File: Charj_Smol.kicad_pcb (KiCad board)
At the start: 2 copper layers, 15 x 15 mm, 18 parts, among them J1 Battery Connector, Q1 PMN30XPEX, U1 MCP73831-2-OT, U2 LC709203FXE-05MH

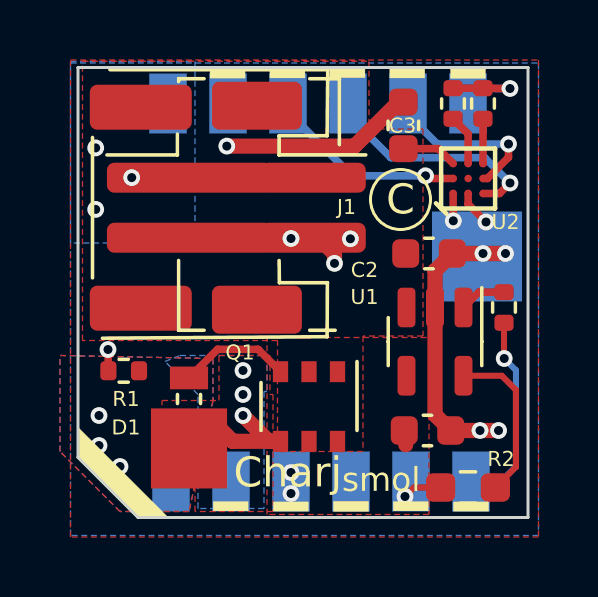
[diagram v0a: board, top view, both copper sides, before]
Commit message: Silkscreen tidying; still Rev C
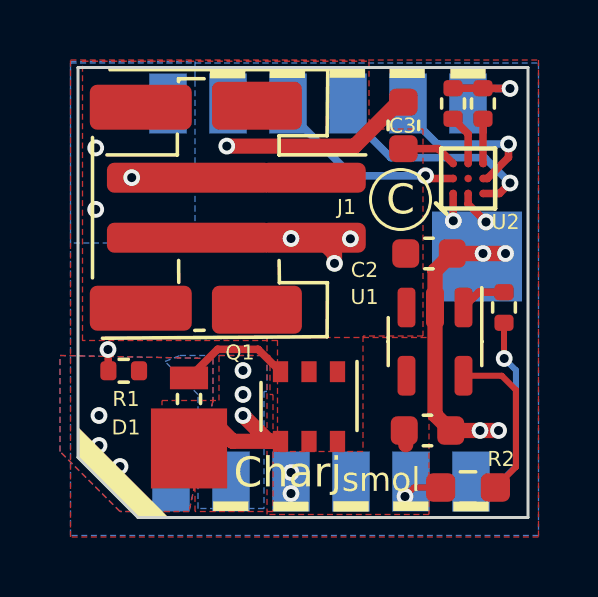
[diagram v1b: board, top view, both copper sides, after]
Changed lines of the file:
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@@
       (effects (font (size 1 1) (thickness 0.15)))
     )
-    (fp_line (start 2.51 -4.2) (end 3.5 -4.2) (layer "F.SilkS") (width 0.12))
+    (fp_line (start -4.15 -4.5) (end 3.1125 -4.5) (layer "F.SilkS") (width 0.12))
+    (fp_line (start 1.4894 -2.3) (end 1.4894 -1.66) (layer "F.SilkS") (width 0.12))
+    (fp_line (start 1.4894 -1.66) (end 4.3794 -1.66) (layer "F.SilkS") (width 0.12))
+    (fp_line (start -4.7306 -2.24) (end -4.7306 2.44) (layer "F.SilkS") (width 0.12))
+    (fp_line (start 3.1125 -4.5) (end 3.0894 -2.3) (layer "F.SilkS") (width 0.12))
+    (fp_line (start 3.0894 -2.3) (end 1.4894 -2.3) (layer "F.SilkS") (width 0.12))
+    (fp_line (start -4.4 4.45) (end 3.0894 4.4) (layer "F.SilkS") (width 0.12))
+    (fp_line (start -1.86 -4.2) (end -1.86 -4.1) (layer "F.SilkS") (width 0.12))
+    (fp_line (start 3.0894 4.4) (end 3.1 2.6) (layer "F.SilkS") (width 0.12))
+    (fp_line (start -1.8542 2.5908) (end -1.86 1.86) (layer "F.SilkS") (width 0.12))
+    (fp_line (start -1.01 -4.2) (end -1.86 -4.2) (layer "F.SilkS") (width 0.12))
+    (fp_line (start -1.9 -1.66) (end -4.25 -1.66) (layer "F.SilkS") (width 0.12))
     (fp_line (start -1.9 -1.66) (end -1.9 -2.35) (layer "F.SilkS") (width 0.12))
-    (fp_line (start 1.4894 -2.3) (end 1.4894 -1.66) (layer "F.SilkS") (width 0.12))
+    (fp_line (start -1.01 4.185) (end -1.3208 4.191) (layer "F.SilkS") (width 0.12))
+    (fp_line (start 3.1 2.6) (end 1.5 2.6) (layer "F.SilkS") (width 0.12))
     (fp_line (start 1.5 2.6) (end 1.4894 1.86) (layer "F.SilkS") (width 0.12))
-    (fp_line (start -4.15 -4.5) (end 3.1125 -4.5) (layer "F.SilkS") (width 0.12))
-    (fp_line (start -1.01 4.185) (end -1.86 4.185) (layer "F.SilkS") (width 0.12))
-    (fp_line (start 3.1125 -4.5) (end 3.0894 -2.3) (layer "F.SilkS") (width 0.12))
-    (fp_line (start 3.0894 4.4) (end 3.1 2.6) (layer "F.SilkS") (width 0.12))
-    (fp_line (start 3.36 4.185) (end 2.51 4.185) (layer "F.SilkS") (width 0.12))
-    (fp_line (start 3.1 2.6) (end 1.5 2.6) (layer "F.SilkS") (width 0.12))
-    (fp_line (start -1.01 -4.2) (end -1.86 -4.2) (layer "F.SilkS") (width 0.12))
-    (fp_line (start -1.86 4.185) (end -1.86 1.86) (layer "F.SilkS") (width 0.12))
-    (fp_line (start -4.7306 -2.24) (end -4.7306 2.44) (layer "F.SilkS") (width 0.12))
-    (fp_line (start -4.4 4.45) (end 3.0894 4.4) (layer "F.SilkS") (width 0.12))
-    (fp_line (start 3.0894 -2.3) (end 1.4894 -2.3) (layer "F.SilkS") (width 0.12))
-    (fp_line (start 1.4894 -1.66) (end 4.3794 -1.66) (layer "F.SilkS") (width 0.12))
-    (fp_line (start -1.86 -4.2) (end -1.86 -4.1) (layer "F.SilkS") (width 0.12))
-    (fp_line (start -1.9 -1.66) (end -4.25 -1.66) (layer "F.SilkS") (width 0.12))
-    (fp_line (start 3.5 -4.2) (end 3.5 -2) (layer "F.SilkS") (width 0.12))
     (fp_rect (start 4.8794 -4.6) (end -5.35 4.8) (layer "F.CrtYd") (width 0.05) (fill none))
+    (fp_line (start 1.3794 -1.4) (end 0.672293 -0.9) (layer "F.Fab") (width 0.1))
+    (fp_line (start 2.9794 -3.85) (end -4.6206 -3.85) (layer "F.Fab") (width 0.1))
+    (fp_line (start 2.9794 3.25) (end 2.9794 4.05) (layer "F.Fab") (width 0.1))
+    (fp_line (start 2.9794 -3.85) (end 2.9794 -3.05) (layer "F.Fab") (width 0.1))
+    (fp_line (start -1.75 -3.875) (end -1.75 4.075) (layer "F.Fab") (width 0.1))
+    (fp_line (start 1.25 0.85) (end 1.25 1.35) (layer "F.Fab") (width 0.1))
+    (fp_line (start -1.75 4.075) (end 3.25 4.075) (layer "F.Fab") (width 0.1))
+    (fp_line (start -1.75 -3.875) (end 3.25 -3.875) (layer "F.Fab") (width 0.1))
+    (fp_line (start 1.3794 -3.05) (end 1.3794 3.25) (layer "F.Fab") (width 0.1))
+    (fp_line (start -4.6206 -3.85) (end -4.6206 4.05) (layer "F.Fab") (width 0.1))
+    (fp_line (start 1.75 -0.65) (end 1.75 -1.15) (layer "F.Fab") (width 0.1))
+    (fp_line (start 1.3794 3.25) (end 2.9794 3.25) (layer "F.Fab") (width 0.1))
     (fp_line (start 0.672293 -0.9) (end 1.3794 -0.4) (layer "F.Fab") (width 0.1))
+    (fp_line (start 1.25 -1.15) (end 1.25 -0.65) (layer "F.Fab") (width 0.1))
     (fp_line (start 1.25 -0.65) (end 1.75 -0.65) (layer "F.Fab") (width 0.1))
-    (fp_line (start 1.3794 -3.05) (end 1.3794 3.25) (layer "F.Fab") (width 0.1))
+    (fp_line (start 1.75 -1.15) (end 1.25 -1.15) (layer "F.Fab") (width 0.1))
+    (fp_line (start 1.25 1.35) (end 1.75 1.35) (layer "F.Fab") (width 0.1))
+    (fp_line (start 1.75 1.35) (end 1.75 0.85) (layer "F.Fab") (width 0.1))
+    (fp_line (start 2.9794 4.05) (end -4.6206 4.05) (layer "F.Fab") (width 0.1))
+    (fp_line (start 2.9794 -3.05) (end 1.3794 -3.05) (layer "F.Fab") (width 0.1))
+    (fp_line (start -1.042893 -0.9) (end -1.75 -0.4) (layer "F.Fab") (width 0.1))
+    (fp_line (start -1.75 -1.4) (end -1.042893 -0.9) (layer "F.Fab") (width 0.1))
     (fp_line (start 3.25 -3.875) (end 3.25 4.075) (layer "F.Fab") (width 0.1))
-    (fp_line (start 1.75 -0.65) (end 1.75 -1.15) (layer "F.Fab") (width 0.1))
-    (fp_line (start 1.25 -1.15) (end 1.25 -0.65) (layer "F.Fab") (width 0.1))
-    (fp_line (start 1.3794 3.25) (end 2.9794 3.25) (layer "F.Fab") (width 0.1))
-    (fp_line (start 2.9794 3.25) (end 2.9794 4.05) (layer "F.Fab") (width 0.1))
     (fp_line (start 1.75 0.85) (end 1.25 0.85) (layer "F.Fab") (width 0.1))
-    (fp_line (start 1.75 -1.15) (end 1.25 -1.15) (layer "F.Fab") (width 0.1))
-    (fp_line (start 1.75 1.35) (end 1.75 0.85) (layer "F.Fab") (width 0.1))
-    (fp_line (start 1.25 0.85) (end 1.25 1.35) (layer "F.Fab") (width 0.1))
-    (fp_line (start -1.042893 -0.9) (end -1.75 -0.4) (layer "F.Fab") (width 0.1))
-    (fp_line (start 2.9794 -3.85) (end -4.6206 -3.85) (layer "F.Fab") (width 0.1))
-    (fp_line (start -1.75 -3.875) (end -1.75 4.075) (layer "F.Fab") (width 0.1))
-    (fp_line (start 1.3794 -1.4) (end 0.672293 -0.9) (layer "F.Fab") (width 0.1))
-    (fp_line (start 2.9794 -3.85) (end 2.9794 -3.05) (layer "F.Fab") (width 0.1))
-    (fp_line (start -1.75 -1.4) (end -1.042893 -0.9) (layer "F.Fab") (width 0.1))
-    (fp_line (start 2.9794 4.05) (end -4.6206 4.05) (layer "F.Fab") (width 0.1))
-    (fp_line (start -1.75 4.075) (end 3.25 4.075) (layer "F.Fab") (width 0.1))
-    (fp_line (start 2.9794 -3.05) (end 1.3794 -3.05) (layer "F.Fab") (width 0.1))
-    (fp_line (start -4.6206 -3.85) (end -4.6206 4.05) (layer "F.Fab") (width 0.1))
-    (fp_line (start -1.75 -3.875) (end 3.25 -3.875) (layer "F.Fab") (width 0.1))
-    (fp_line (start 1.25 1.35) (end 1.75 1.35) (layer "F.Fab") (width 0.1))
     (pad "1" smd roundrect (at -1.5 -0.9 270) (size 1 5.5) (layers "F.Cu" "F.Paste" "F.Mask") (roundrect_rratio 0.25)
       (net 1 "+BATT") (pinfunction "Pin_1") (pintype "passive"))
     (pad "1" smd roundrect (at 2.6294 -0.9 270) (size 1 3.5) (layers "F.Cu" "F.Paste" "F.Mask") (roundrect_rratio 0.25)
       (net 1 "+BATT") (pinfunction "Pin_1") (pintype "passive"))
+    (pad "2" smd roundrect (at 2.6294 1.1 270) (size 1 3.5) (layers "F.Cu" "F.Paste" "F.Mask") (roundrect_rratio 0.25)
+      (net 2 "GND") (pinfunction "Pin_2") (pintype "passive"))
     (pad "2" smd roundrect (at -1.5 1.1 270) (size 1 5.5) (layers "F.Cu" "F.Paste" "F.Mask") (roundrect_rratio 0.25)
       (net 2 "GND") (pinfunction "Pin_2") (pintype "passive"))
-    (pad "2" smd roundrect (at 2.6294 1.1 270) (size 1 3.5) (layers "F.Cu" "F.Paste" "F.Mask") (roundrect_rratio 0.25)
-      (net 2 "GND") (pinfunction "Pin_2") (pintype "passive"))
-    (pad "MP" smd roundrect (at -3.1206 -3.25 270) (size 1.5 3.4) (layers "F.Cu" "F.Paste" "F.Mask") (roundrect_rratio 0.1666673333))
     (pad "MP" smd roundrect (at 0.75 3.5 270) (size 1.6 3) (layers "F.Cu" "F.Paste" "F.Mask") (roundrect_rratio 0.15625))
-    (pad "MP" smd roundrect (at -3.1206 3.45 270) (size 1.5 3.4) (layers "F.Cu" "F.Paste" "F.Mask") (roundrect_rratio 0.1666673333))
+    (pad "MP" smd roundrect (at -3.1206 -3.25 270) (size 1.5 3.4) (layers "F.Cu" "F.Paste" "F.Mask") (roundrect_rratio 0.166667))
+    (pad "MP" smd roundrect (at -3.1206 3.45 270) (size 1.5 3.4) (layers "F.Cu" "F.Paste" "F.Mask") (roundrect_rratio 0.166667))
     (pad "MP" smd roundrect (at 0.75 -3.3 270) (size 1.6 3) (layers "F.Cu" "F.Paste" "F.Mask") (roundrect_rratio 0.15625))
     (model "${MODELSPATH}/JST/S2B-PH-SM4-TB.STEP"
@@
       (rotate (xyz -90 0 90))
     )
-    (model "${MODELSPATH}/JST/B2B-PH-SM4-TB.STEP"
+    (model "${MODELSPATH}/JST/B2B-PH-SM4-TB.STEP" hide
       (offset (xyz 2.25 3.85 0))
       (scale (xyz 1 1 1))
@@
     (property "Sheetfile" "Charj_Smol.kicad_sch")
     (property "Sheetname" "")
-    (attr smd)
+    (property "exclude_from_bom" "")
+    (attr smd exclude_from_bom)
     (fp_text reference "PADS3" (at 0 4 unlocked) (layer "B.SilkS") hide
       (effects (font (size 1 1) (thickness 0.15)) (justify mirror))
@@
     (property "Sheetfile" "Charj_Smol.kicad_sch")
     (property "Sheetname" "")
-    (attr smd)
+    (property "exclude_from_bom" "")
+    (attr smd exclude_from_bom)
     (fp_text reference "PADS1" (at 0.5 3.8 180 unlocked) (layer "B.Fab")
       (effects (font (size 1 1) (thickness 0.15)) (justify mirror))
@@
     (property "Sheetfile" "Charj_Smol.kicad_sch")
     (property "Sheetname" "")
-    (attr smd)
+    (property "exclude_from_bom" "")
+    (attr smd exclude_from_bom)
     (fp_text reference "PADS2" (at 0.5 3.8 unlocked) (layer "B.Fab")
       (effects (font (size 1 1) (thickness 0.15)) (justify mirror))
